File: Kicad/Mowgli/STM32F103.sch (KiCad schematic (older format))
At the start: 1 part

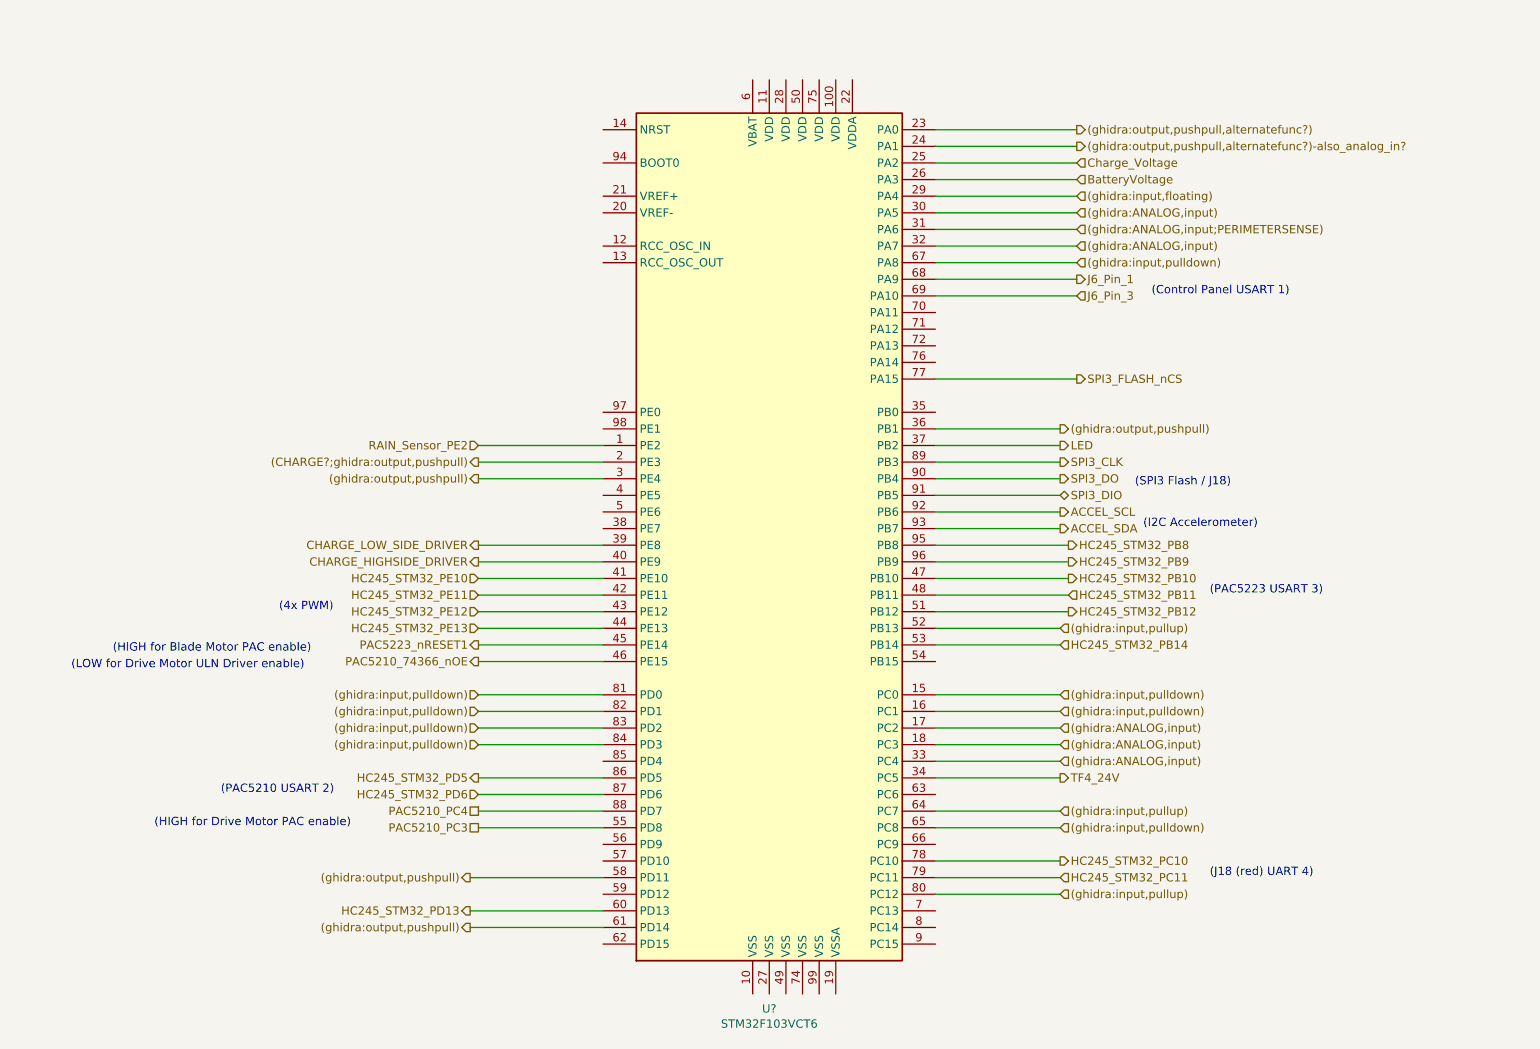
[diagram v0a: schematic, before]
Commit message: added some datasheets, kicad updates
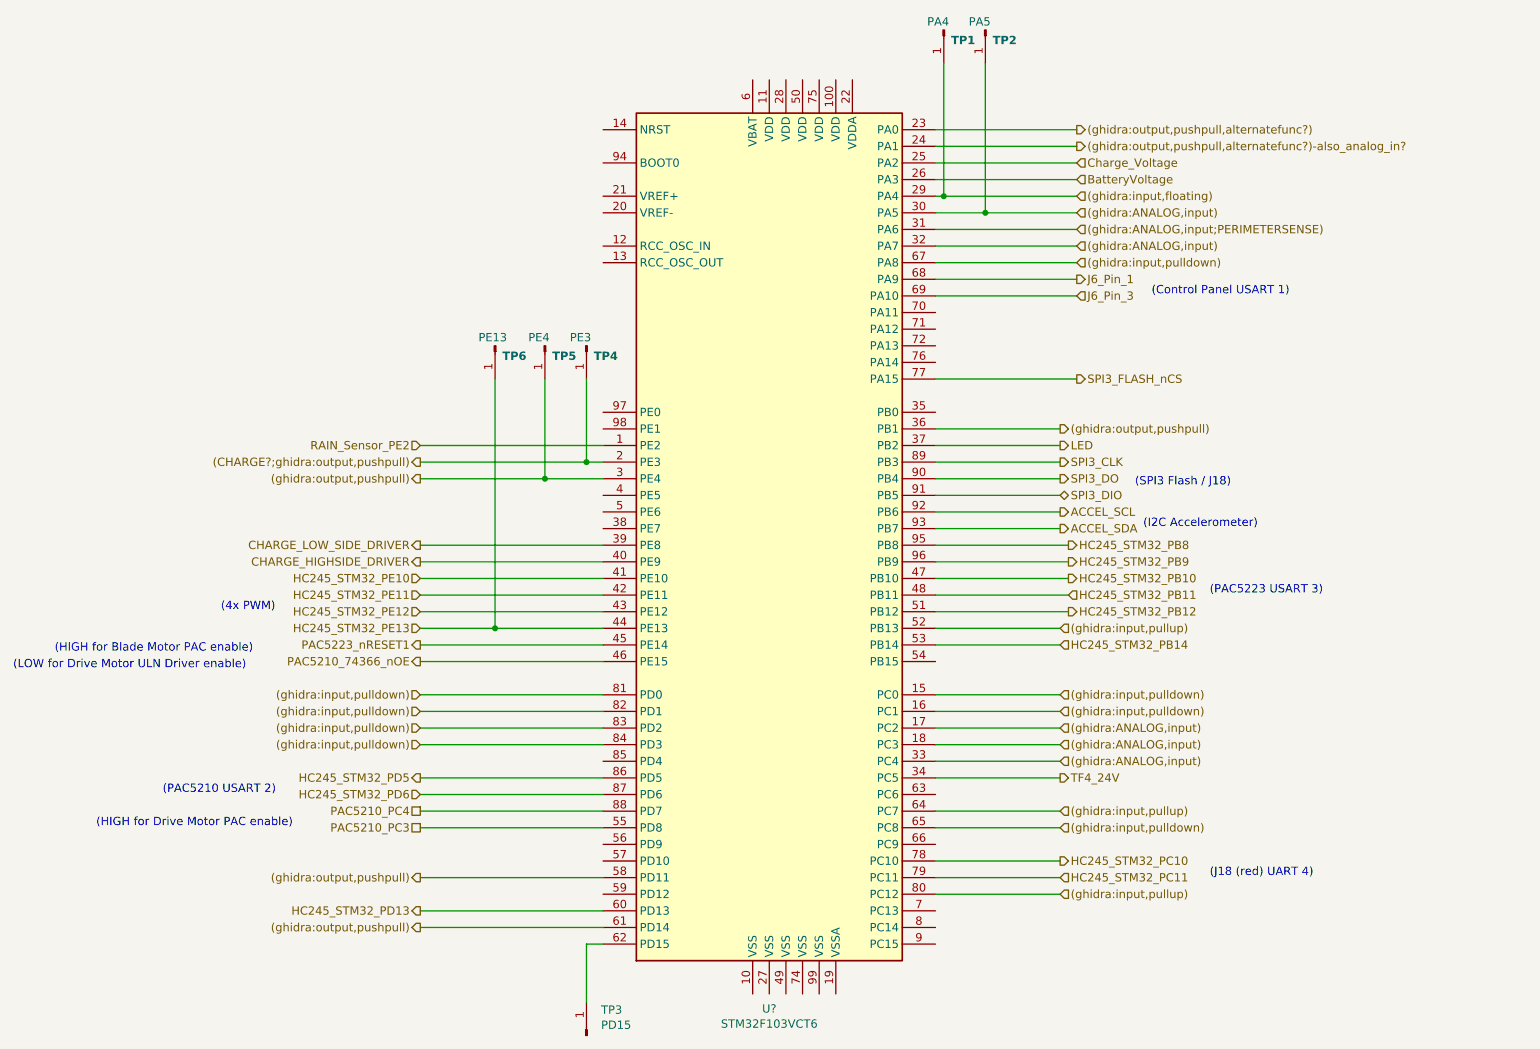
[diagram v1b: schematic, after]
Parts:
- added TP1: PA4, symbol Connector:Conn_01x01_Male
- added TP2: PA5, symbol Connector:Conn_01x01_Male
- added TP3: PD15, symbol Connector:Conn_01x01_Male
- added TP4: PE3, symbol Connector:Conn_01x01_Male
- added TP5: PE4, symbol Connector:Conn_01x01_Male
- added TP6: PE13, symbol Connector:Conn_01x01_Male
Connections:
- net (CHARGE?;ghidra:output,pushpull): now also TP4.1 (Pin_1)
- net (ghidra:ANALOG,input): now also TP2.1 (Pin_1)
- net (ghidra:input,floating): now also TP1.1 (Pin_1)
- net (ghidra:output,pushpull): now also TP5.1 (Pin_1)
- net HC245_STM32_PE13: now also TP6.1 (Pin_1)
- net at U?.62 (PD15): now also TP3.1 (Pin_1)
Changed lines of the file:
@@
 $Descr A4 11693 8268
 encoding utf-8
-Sheet 3 12
+Sheet 3 13
 Title "Project Mowgli"
 Date "2022-05-22"
@@
 	1    0    0    -1
 $EndComp
-Text HLabel 3700 4500 0    50   Output ~ 0
+Text HLabel 3350 4500 0    50   Output ~ 0
 PAC5223_nRESET1
-Wire Wire Line
-	4450 4500 3700 4500
-Text HLabel 3700 5500 0    50   UnSpc ~ 0
+Text HLabel 3350 5500 0    50   UnSpc ~ 0
 PAC5210_PC4
-Wire Wire Line
-	4450 5500 3700 5500
-Text HLabel 3700 4600 0    50   Output ~ 0
+Text HLabel 3350 4600 0    50   Output ~ 0
 PAC5210_74366_nOE
-Wire Wire Line
-	4450 4600 3700 4600
-Text HLabel 3700 5600 0    50   UnSpc ~ 0
+Text HLabel 3350 5600 0    50   UnSpc ~ 0
 PAC5210_PC3
-Wire Wire Line
-	4450 5600 3700 5600
 Text HLabel 7200 5300 2    50   Output ~ 0
 TF4_24V
@@
 Wire Wire Line
 	7200 3300 6450 3300
-Text HLabel 3700 4100 0    50   Input ~ 0
+Text HLabel 3350 4100 0    50   Input ~ 0
 HC245_STM32_PE10
-Wire Wire Line
-	4450 4100 3700 4100
-Text HLabel 3700 4300 0    50   Input ~ 0
+Text HLabel 3350 4300 0    50   Input ~ 0
 HC245_STM32_PE12
-Text HLabel 3700 4400 0    50   Input ~ 0
+Text HLabel 3350 4400 0    50   Input ~ 0
 HC245_STM32_PE13
-Wire Wire Line
-	4450 4200 3700 4200
-Text HLabel 3700 4200 0    50   Input ~ 0
+Text HLabel 3350 4200 0    50   Input ~ 0
 HC245_STM32_PE11
 Wire Wire Line
-	4450 4300 3700 4300
-Wire Wire Line
-	4450 4400 3700 4400
+	4450 4400 3800 4400
 Text HLabel 7200 4500 2    50   Input ~ 0
 HC245_STM32_PB14
 Wire Wire Line
 	7200 4500 6450 4500
-Text HLabel 3650 6100 0    50   Output ~ 0
+Text HLabel 3350 6100 0    50   Output ~ 0
 HC245_STM32_PD13
-Wire Wire Line
-	4450 6100 3650 6100
 Text HLabel 7250 3900 2    50   Output ~ 0
 HC245_STM32_PB8
@@
 Wire Wire Line
 	7250 4300 6450 4300
-Text Notes 1750 5600 0    50   ~ 0
+Text Notes 1400 5600 0    50   ~ 0
 (HIGH for Drive Motor PAC enable)
-Text Notes 1250 4650 0    50   ~ 0
+Text Notes 900  4650 0    50   ~ 0
 (LOW for Drive Motor ULN Driver enable)
-Text Notes 1500 4550 0    50   ~ 0
+Text Notes 1150 4550 0    50   ~ 0
 (HIGH for Blade Motor PAC enable)
-Text HLabel 3700 5300 0    50   Output ~ 0
+Text HLabel 3350 5300 0    50   Output ~ 0
 HC245_STM32_PD5
-Text HLabel 3700 5400 0    50   Input ~ 0
+Text HLabel 3350 5400 0    50   Input ~ 0
 HC245_STM32_PD6
-Wire Wire Line
-	4450 5300 3700 5300
-Wire Wire Line
-	4450 5400 3700 5400
-Text Notes 2150 5400 0    50   ~ 0
+Text Notes 1800 5400 0    50   ~ 0
 (PAC5210 USART 2)
 Text HLabel 7250 4100 2    50   Output ~ 0
@@
 Text Notes 8100 5900 0    50   ~ 0
 (J18 (red) UART 4)
-Text Notes 2500 4300 0    50   ~ 0
+Text Notes 2150 4300 0    50   ~ 0
 (4x PWM)
 Text HLabel 7300 2300 2    50   Output ~ 0
@@
 Text Notes 7650 3550 0    50   ~ 0
 (SPI3 Flash / J18)
-Text HLabel 3700 3900 0    50   Output ~ 0
+Text HLabel 3350 3900 0    50   Output ~ 0
 CHARGE_LOW_SIDE_DRIVER
-Text HLabel 3700 4000 0    50   Output ~ 0
+Text HLabel 3350 4000 0    50   Output ~ 0
 CHARGE_HIGHSIDE_DRIVER
-Wire Wire Line
-	4450 3900 3700 3900
-Wire Wire Line
-	4450 4000 3700 4000
 Wire Wire Line
 	7300 1700 6450 1700
@@
 Wire Wire Line
 	7300 2200 6450 2200
-Text HLabel 3700 5000 0    50   Input ~ 0
-(ghidra:input,pulldown)
-Text HLabel 3700 5100 0    50   Input ~ 0
-(ghidra:input,pulldown)
-Wire Wire Line
-	4450 5100 3700 5100
-Wire Wire Line
-	3700 5000 4450 5000
-Text HLabel 3700 4900 0    50   Input ~ 0
-(ghidra:input,pulldown)
-Text HLabel 3700 4800 0    50   Input ~ 0
-(ghidra:input,pulldown)
-Wire Wire Line
-	4450 4800 3700 4800
-Wire Wire Line
-	4450 4900 3700 4900
+Text HLabel 3350 5000 0    50   Input ~ 0
+(ghidra:input,pulldown)
+Text HLabel 3350 5100 0    50   Input ~ 0
+(ghidra:input,pulldown)
+Text HLabel 3350 4900 0    50   Input ~ 0
+(ghidra:input,pulldown)
+Text HLabel 3350 4800 0    50   Input ~ 0
+(ghidra:input,pulldown)
 Text HLabel 7300 1400 2    50   Output ~ 0
 (ghidra:output,pushpull,alternatefunc?)
@@
 	6450 2000 7300 2000
 Wire Wire Line
-	7300 1900 6450 1900
+	7300 1900 6750 1900
 Text HLabel 7200 5000 2    50   Input ~ 0
 (ghidra:ANALOG,input)
@@
 Wire Wire Line
 	7200 5600 6450 5600
-Text HLabel 3700 3300 0    50   Input ~ 0
+Text HLabel 3350 3300 0    50   Input ~ 0
 RAIN_Sensor_PE2
-Wire Wire Line
-	4450 3300 3700 3300
 Text HLabel 7200 6000 2    50   Input ~ 0
 (ghidra:input,pullup)
 Wire Wire Line
 	7200 6000 6450 6000
-Text HLabel 3650 6200 0    50   Output ~ 0
+Text HLabel 3350 6200 0    50   Output ~ 0
 (ghidra:output,pushpull)
-Wire Wire Line
-	4450 6200 3650 6200
-Text HLabel 3650 5900 0    50   Output ~ 0
+Text HLabel 3350 5900 0    50   Output ~ 0
 (ghidra:output,pushpull)
-Wire Wire Line
-	4450 5900 3650 5900
-Text HLabel 3700 3400 0    50   Output ~ 0
+Text HLabel 3350 3400 0    50   Output ~ 0
 (CHARGE?;ghidra:output,pushpull)
 Wire Wire Line
-	4450 3400 3700 3400
-Text HLabel 3700 3500 0    50   Output ~ 0
+	4450 3400 4350 3400
+Text HLabel 3350 3500 0    50   Output ~ 0
 (ghidra:output,pushpull)
-Wire Wire Line
-	4450 3500 3700 3500
 Text HLabel 7300 1800 2    50   Input ~ 0
 (ghidra:input,floating)
 Wire Wire Line
-	7300 1800 6450 1800
+	7300 1800 6500 1800
 Text HLabel 7300 1700 2    50   Input ~ 0
 BatteryVoltage
 Text HLabel 7300 1600 2    50   Input ~ 0
 Charge_Voltage
+$Comp
+L Connector:Conn_01x01_Male TP6
+U 1 1 62BD479C
+P 3800 2700
+F 0 "TP6" V 3862 2744 50  0000 L CNB
+F 1 "PE13" V 3750 2600 50  0000 L CNN
+F 2 "" H 3800 2700 50  0001 C CNN
+F 3 "~" H 3800 2700 50  0001 C CNN
+	1    3800 2700
+	0    1    1    0
+$EndComp
+Wire Wire Line
+	3800 2900 3800 4400
+$Comp
+L Connector:Conn_01x01_Male TP1
+U 1 1 62BDB441
+P 6500 800
+F 0 "TP1" V 6562 844 50  0000 L CNB
+F 1 "PA4" V 6450 700 50  0000 L CNN
+F 2 "" H 6500 800 50  0001 C CNN
+F 3 "~" H 6500 800 50  0001 C CNN
+	1    6500 800
+	0    1    1    0
+$EndComp
+Wire Wire Line
+	6500 1000 6500 1800
+Connection ~ 6500 1800
+Wire Wire Line
+	6500 1800 6450 1800
+$Comp
+L Connector:Conn_01x01_Male TP2
+U 1 1 62BDDD40
+P 6750 800
+F 0 "TP2" V 6812 844 50  0000 L CNB
+F 1 "PA5" V 6700 700 50  0000 L CNN
+F 2 "" H 6750 800 50  0001 C CNN
+F 3 "~" H 6750 800 50  0001 C CNN
+	1    6750 800
+	0    1    1    0
+$EndComp
+Wire Wire Line
+	6750 1000 6750 1900
+Connection ~ 6750 1900
+Wire Wire Line
+	6750 1900 6450 1900
+$Comp
+L Connector:Conn_01x01_Male TP3
+U 1 1 62BE0448
+P 4350 6850
+F 0 "TP3" V 4504 6762 50  0000 R CNN
+F 1 "PD15" V 4413 6762 50  0000 R CNN
+F 2 "" H 4350 6850 50  0001 C CNN
+F 3 "~" H 4350 6850 50  0001 C CNN
+	1    4350 6850
+	0    -1   -1   0
+$EndComp
+Wire Wire Line
+	4450 6300 4350 6300
+Wire Wire Line
+	4350 6300 4350 6650
+$Comp
+L Connector:Conn_01x01_Male TP5
+U 1 1 62BE67AB
+P 4100 2700
+F 0 "TP5" V 4162 2744 50  0000 L CNB
+F 1 "PE4" V 4050 2600 50  0000 L CNN
+F 2 "" H 4100 2700 50  0001 C CNN
+F 3 "~" H 4100 2700 50  0001 C CNN
+	1    4100 2700
+	0    1    1    0
+$EndComp
+$Comp
+L Connector:Conn_01x01_Male TP4
+U 1 1 62BE9166
+P 4350 2700
+F 0 "TP4" V 4412 2744 50  0000 L CNB
+F 1 "PE3" V 4300 2600 50  0000 L CNN
+F 2 "" H 4350 2700 50  0001 C CNN
+F 3 "~" H 4350 2700 50  0001 C CNN
+	1    4350 2700
+	0    1    1    0
+$EndComp
+Wire Wire Line
+	4350 2900 4350 3400
+Wire Wire Line
+	4100 3500 4450 3500
+Wire Wire Line
+	3350 4400 3800 4400
+Connection ~ 3800 4400
+Wire Wire Line
+	3350 4300 4450 4300
+Wire Wire Line
+	3350 4200 4450 4200
+Wire Wire Line
+	3350 4100 4450 4100
+Wire Wire Line
+	3350 4000 4450 4000
+Wire Wire Line
+	3350 3900 4450 3900
+Wire Wire Line
+	3350 3500 4100 3500
+Connection ~ 4100 3500
+Wire Wire Line
+	3350 3400 4350 3400
+Connection ~ 4350 3400
+Wire Wire Line
+	3350 3300 4450 3300
+Wire Wire Line
+	4100 2900 4100 3500
+Wire Wire Line
+	3350 4500 4450 4500
+Wire Wire Line
+	3350 4600 4450 4600
+Wire Wire Line
+	3350 4800 4450 4800
+Wire Wire Line
+	3350 4900 4450 4900
+Wire Wire Line
+	3350 5000 4450 5000
+Wire Wire Line
+	3350 5100 4450 5100
+Wire Wire Line
+	3350 5300 4450 5300
+Wire Wire Line
+	3350 5400 4450 5400
+Wire Wire Line
+	3350 5500 4450 5500
+Wire Wire Line
+	3350 5600 4450 5600
+Wire Wire Line
+	3350 6200 4450 6200
+Wire Wire Line
+	3350 6100 4450 6100
+Wire Wire Line
+	3350 5900 4450 5900
 $EndSCHEMATC

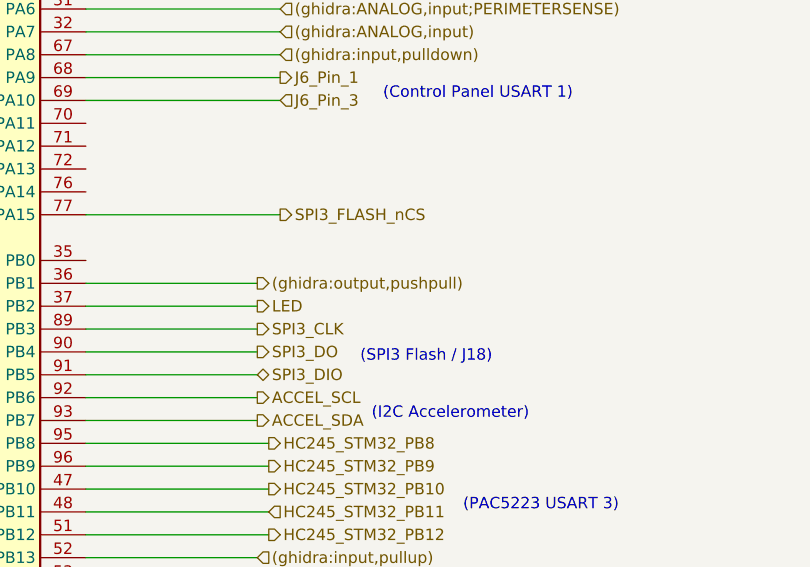
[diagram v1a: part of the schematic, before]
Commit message: added onboard BEEPER
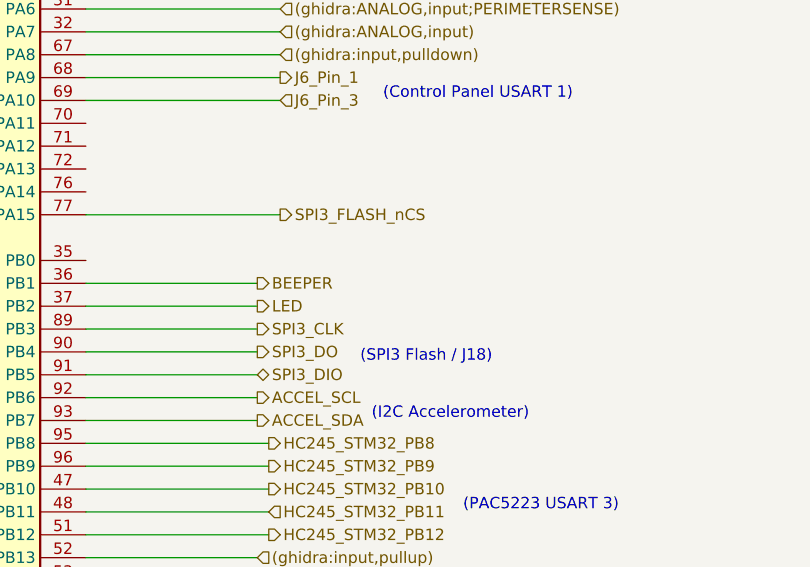
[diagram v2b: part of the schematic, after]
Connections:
- net (ghidra:output,pushpull): no longer U?.36 (PB1)
- new net BEEPER: U?.36 (PB1)
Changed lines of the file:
@@
 $Descr A4 11693 8268
 encoding utf-8
-Sheet 3 13
+Sheet 3 14
 Title "Project Mowgli"
 Date "2022-05-22"
@@
 	7200 5500 6450 5500
 Text HLabel 7200 3200 2    50   Output ~ 0
-(ghidra:output,pushpull)
+BEEPER
 Wire Wire Line
 	7200 3200 6450 3200
